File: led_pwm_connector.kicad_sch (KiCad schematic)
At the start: 7 parts, among them CN7 JST_VH_8PIN_10A_250V

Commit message: commit before updating to LiveAstra lib
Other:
- note added: "If a different signal is required here the 0Ohm + PTH will allow a post assembly fix / experimentation. Otherwise, just GND."
- note added: "Information"

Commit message: Updated library name, updated and verified all footprints
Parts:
- CN7: symbol EASYEDA2KICAD:JST_VH_8PIN_10A_250V -> LiveAstra:JST_VH_8PIN_10A_250V
- R31: symbol EASYEDA2KICAD:R_0Ohm_0805_125mW -> LiveAstra:R_0Ohm_0805_125mW
- TP55, TP56, TP57, TP58, TP59: symbol EASYEDA2KICAD:TestPoint_Thimble -> LiveAstra:TestPoint_Thimble
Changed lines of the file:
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@@
 	)
 	(symbol
-		(lib_id "EASYEDA2KICAD:JST_VH_8PIN_10A_250V")
+		(lib_id "LiveAstra:JST_VH_8PIN_10A_250V")
 		(at 182.88 96.52 0)
 		(unit 1)
@@
 	)
 	(symbol
-		(lib_id "EASYEDA2KICAD:TestPoint_Thimble")
+		(lib_id "LiveAstra:TestPoint_Thimble")
 		(at 121.92 78.74 0)
 		(unit 1)
@@
 	)
 	(symbol
-		(lib_id "EASYEDA2KICAD:+5V_IN")
+		(lib_id "LiveAstra:+5V_IN")
 		(at 172.72 76.2 0)
 		(unit 1)
@@
 	)
 	(symbol
-		(lib_id "EASYEDA2KICAD:R_0Ohm_0805_125mW")
+		(lib_id "LiveAstra:R_0Ohm_0805_125mW")
 		(at 121.92 116.84 0)
 		(unit 1)
@@
 	)
 	(symbol
-		(lib_id "EASYEDA2KICAD:TestPoint_Thimble")
+		(lib_id "LiveAstra:TestPoint_Thimble")
 		(at 86.36 78.74 0)
 		(unit 1)
@@
 	)
 	(symbol
-		(lib_id "EASYEDA2KICAD:TestPoint_Thimble")
+		(lib_id "LiveAstra:TestPoint_Thimble")
 		(at 152.4 78.74 0)
 		(unit 1)
@@
 	)
 	(symbol
-		(lib_id "EASYEDA2KICAD:TestPoint_Thimble")
+		(lib_id "LiveAstra:TestPoint_Thimble")
 		(at 55.88 78.74 0)
 		(unit 1)
@@
 	)
 	(symbol
-		(lib_id "EASYEDA2KICAD:TestPoint_Thimble")
+		(lib_id "LiveAstra:TestPoint_Thimble")
 		(at 139.7 114.3 0)
 		(unit 1)

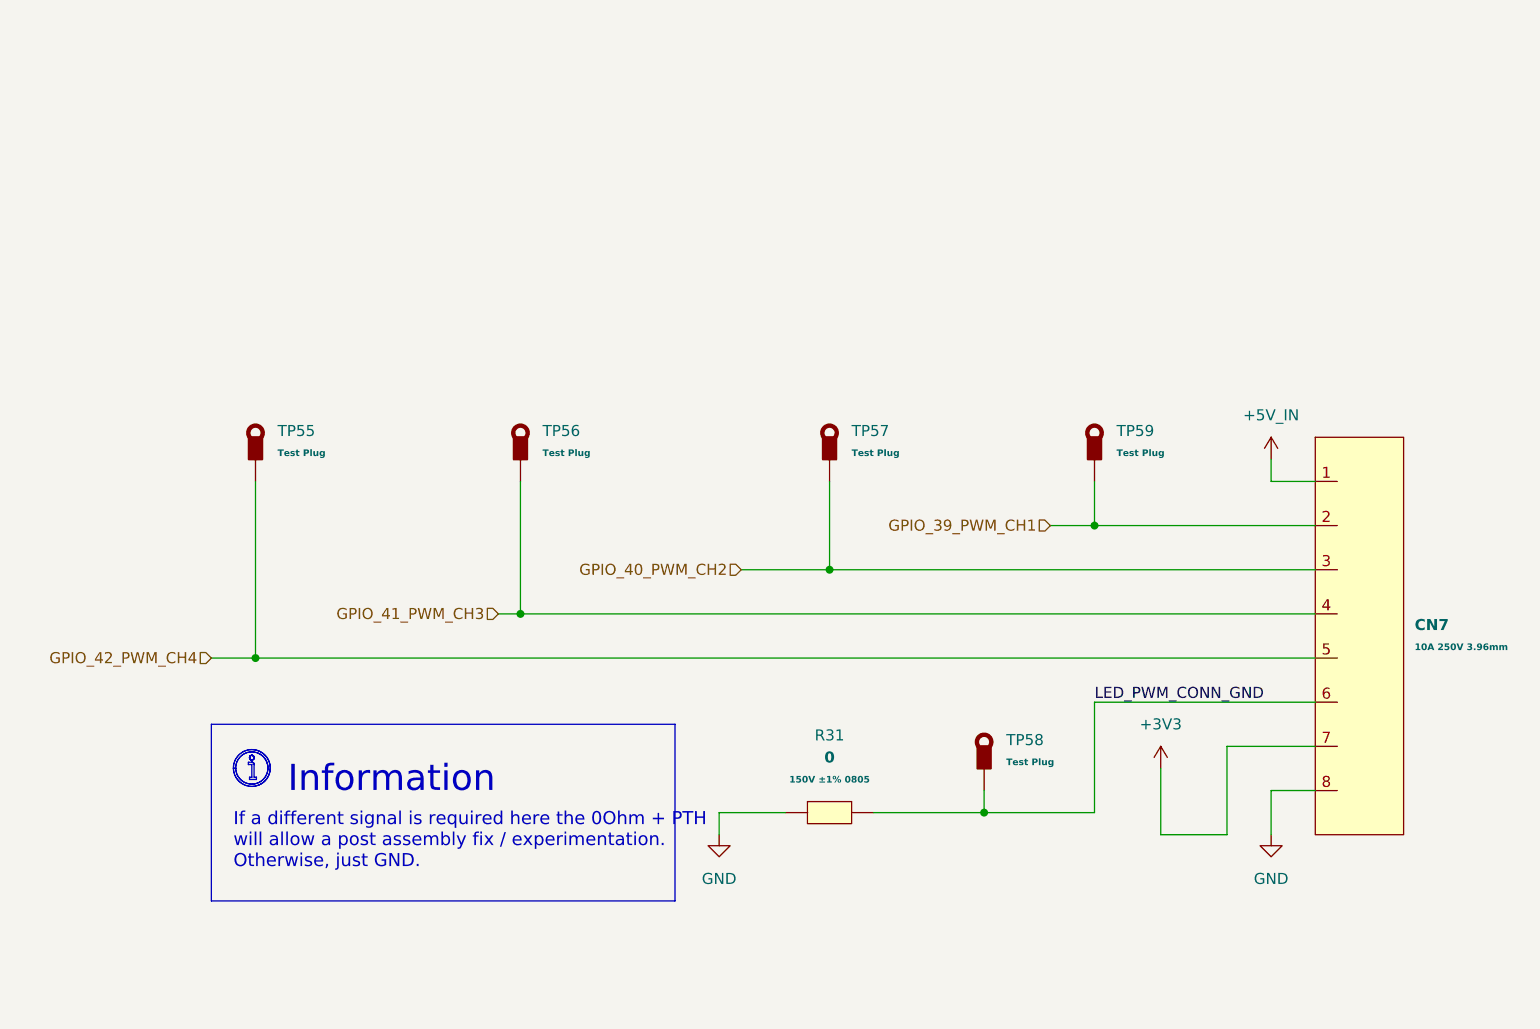
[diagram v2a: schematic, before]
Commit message: Finished layout no drc or erc errors
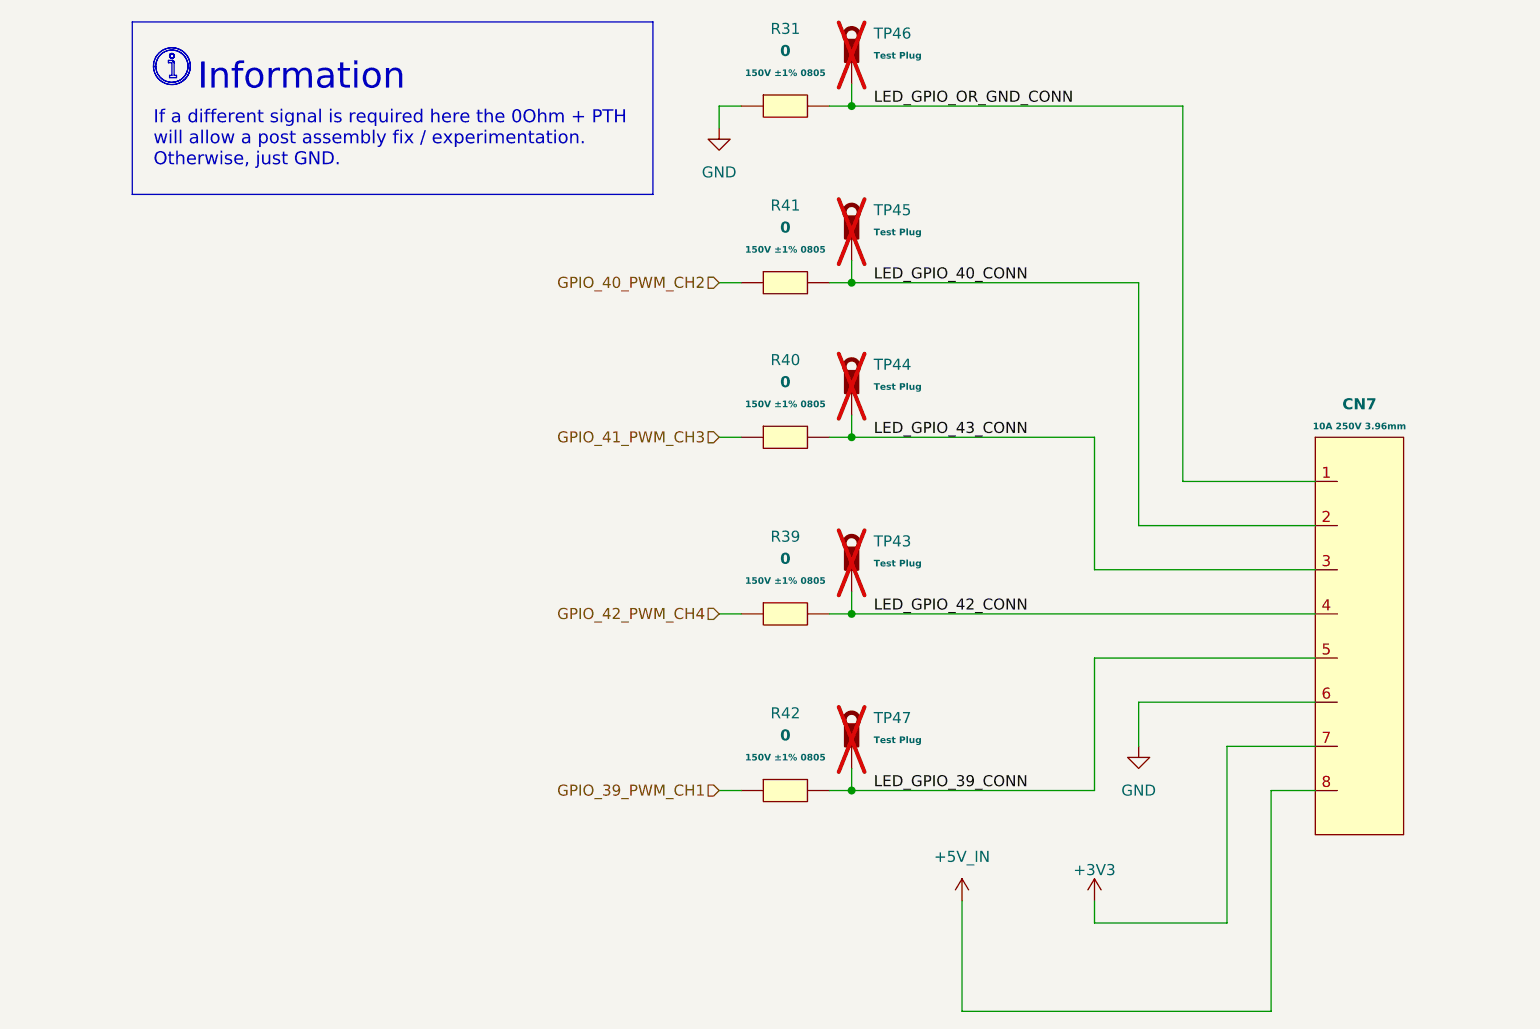
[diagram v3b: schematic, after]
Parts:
- added R39, R40, R41, R42: 0, LiveAstra:R_0805_2012Metric_Pad1.20x1.40mm_HandSolder, symbol LiveAstra:R_0Ohm_0805_125mW
- CN7: footprint Connector_JST:JST_VH_B8P-VH-B_1x08_P3.96mm_Vertical -> LiveAstra:JST_VH_B8P-VH-B_1x08_P3.96mm_Vertical
- R31: footprint Resistor_SMD:R_0805_2012Metric_Pad1.20x1.40mm_HandSolder -> LiveAstra:R_0805_2012Metric_Pad1.20x1.40mm_HandSolder
- TP43: renamed from TP55; footprint TestPoint:TestPoint_Loop_D3.50mm_Drill0.9mm_Beaded -> LiveAstra:TestPoint_Loop_D3.50mm_Drill0.9mm_Beaded; now not fitted; now left out of the parts list
- TP44: renamed from TP56; footprint TestPoint:TestPoint_Loop_D3.50mm_Drill0.9mm_Beaded -> LiveAstra:TestPoint_Loop_D3.50mm_Drill0.9mm_Beaded; now not fitted; now left out of the parts list
- TP45: renamed from TP57; footprint TestPoint:TestPoint_Loop_D3.50mm_Drill0.9mm_Beaded -> LiveAstra:TestPoint_Loop_D3.50mm_Drill0.9mm_Beaded; now not fitted; now left out of the parts list
- TP46: renamed from TP58; footprint TestPoint:TestPoint_Loop_D3.50mm_Drill0.9mm_Beaded -> LiveAstra:TestPoint_Loop_D3.50mm_Drill0.9mm_Beaded; now not fitted; now left out of the parts list
- TP47: renamed from TP59; footprint TestPoint:TestPoint_Loop_D3.50mm_Drill0.9mm_Beaded -> LiveAstra:TestPoint_Loop_D3.50mm_Drill0.9mm_Beaded; now not fitted; now left out of the parts list
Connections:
- net +5V_IN: now also CN7.8; no longer CN7.1
- net GND: now also CN7.6; no longer CN7.8
- net GPIO_39_PWM_CH1: now also R42.1; no longer CN7.2, TP47.1
- net GPIO_40_PWM_CH2: now also R41.1; no longer CN7.3, TP45.1
- net GPIO_41_PWM_CH3: now also R40.1; no longer CN7.4, TP44.1
- net GPIO_42_PWM_CH4: now also R39.1; no longer CN7.5, TP43.1
- net LED_PWM_CONN_GND renamed LED_GPIO_OR_GND_CONN
- net LED_GPIO_OR_GND_CONN: now also CN7.1; no longer CN7.6
- new net LED_GPIO_39_CONN: CN7.5, R42.2, TP47.1
- new net LED_GPIO_40_CONN: CN7.2, R41.2, TP45.1
- new net LED_GPIO_42_CONN: CN7.4, R39.2, TP43.1
- new net LED_GPIO_43_CONN: CN7.3, R40.2, TP44.1
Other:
- moved on the sheet: R31

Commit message: Ready for kibot
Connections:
- net GPIO_39_PWM_CH1 renamed PWM_CH4
- net GPIO_40_PWM_CH2 renamed PWM_CH1
- net GPIO_41_PWM_CH3 renamed PWM_CH2
- net GPIO_42_PWM_CH4 renamed PWM_CH3
- net LED_GPIO_39_CONN renamed PWM_CH4_CONN
- net LED_GPIO_40_CONN renamed PWM_CH1_CONN
- net LED_GPIO_42_CONN renamed PWM_CH3_CONN
- net LED_GPIO_43_CONN renamed PWM_CH2_CONN
- net LED_GPIO_OR_GND_CONN renamed LED_EXTRA_PIN
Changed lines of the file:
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@@
 		)
 	)
-	(label "LED_GPIO_39_CONN"
+	(label "PWM_CH4_CONN"
 		(at 127 114.3 0)
 		(fields_autoplaced yes)
@@
 		)
 	)
-	(label "LED_GPIO_40_CONN"
+	(label "PWM_CH1_CONN"
 		(at 127 55.88 0)
 		(fields_autoplaced yes)
@@
 		)
 	)
-	(label "LED_GPIO_OR_GND_CONN"
+	(label "LED_EXTRA_PIN"
 		(at 127 35.56 0)
 		(fields_autoplaced yes)
@@
 		)
 	)
-	(label "LED_GPIO_42_CONN"
+	(label "PWM_CH3_CONN"
 		(at 127 93.98 0)
 		(fields_autoplaced yes)
@@
 		)
 	)
-	(label "LED_GPIO_43_CONN"
+	(label "PWM_CH2_CONN"
 		(at 127 73.66 0)
 		(fields_autoplaced yes)
@@
 		)
 	)
-	(hierarchical_label "GPIO_41_PWM_CH3"
+	(hierarchical_label "PWM_CH3"
+		(shape input)
+		(at 109.22 93.98 180)
+		(fields_autoplaced yes)
+		(effects
+			(font
+				(size 1.27 1.27)
+			)
+			(justify right)
+		)
+	)
+	(hierarchical_label "PWM_CH2"
 		(shape input)
 		(at 109.22 73.66 180)
@@
 		)
 	)
-	(hierarchical_label "GPIO_42_PWM_CH4"
+	(hierarchical_label "PWM_CH4"
 		(shape input)
-		(at 109.22 93.98 180)
+		(at 109.22 114.3 180)
 		(fields_autoplaced yes)
 		(effects
@@
 		)
 	)
-	(hierarchical_label "GPIO_40_PWM_CH2"
+	(hierarchical_label "PWM_CH1"
 		(shape input)
 		(at 109.22 55.88 180)
 		(fields_autoplaced yes)
 		(effects
-			(font
-				(size 1.27 1.27)
-			)
-			(justify right)
-		)
-	)
-	(hierarchical_label "GPIO_39_PWM_CH1"
-		(shape input)
-		(at 109.22 114.3 180)
-		(fields_autoplaced yes)
-		(effects

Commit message: Work on kibot
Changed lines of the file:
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@@
-		)
-	)
-	(polyline
-		(pts
-			(xy 46.2731 30.3055) (xy 46.2861 30.3065) (xy 46.299 30.3081) (xy 46.3118 30.3103) (xy 46.3245 30.3132)
-			(xy 46.3369 30.3166) (xy 46.3492 30.3207) (xy 46.3612 30.3253) (xy 46.373 30.3306) (xy 46.3846 30.3364)
-			(xy 46.3958 30.3427) (xy 46.4068 30.3497) (xy 46.4174 30.3571) (xy 46.4276 30.3651) (xy 46.4375 30.3737)
-			(xy 46.4471 30.3827) (xy 46.4561 30.3922) (xy 46.4646 30.4021) (xy 46.4726 30.4124) (xy 46.4801 30.423)
-			(xy 46.487 30.4339) (xy 46.4934 30.4452) (xy 46.4992 30.4567) (xy 46.5044 30.4685) (xy 46.5091 30.4806)
-			(xy 46.5131 30.4928) (xy 46.5166 30.5053) (xy 46.5194 30.5179) (xy 46.5217 30.5307) (xy 46.5233 30.5436)
-			(xy 46.5242 30.5567) (xy 46.5245 30.5698) (xy 46.5245 32.025) (xy 46.7891 32.025) (xy 46.7891 32.2896)
-			(xy 45.9954 32.2896) (xy 45.9954 32.025) (xy 46.26 32.025) (xy 46.26 30.5698) (xy 45.8631 30.5698)
-			(xy 45.8631 30.3052) (xy 46.26 30.3052) (xy 46.2731 30.3055)
-		)
-		(stroke
-			(width -0.0001)
-			(type solid)
-		)
-		(fill
-			(type color)
-			(color 34 187 51 1)
-		)
-	)
-	(polyline
-		(pts
-			(xy 46.2736 29.5118) (xy 46.287 29.5128) (xy 46.3003 29.5145) (xy 46.3133 29.5168) (xy 46.3261 29.5198)
-			(xy 46.3386 29.5234) (xy 46.3509 29.5275) (xy 46.363 29.5323) (xy 46.3747 29.5375) (xy 46.3861 29.5434)
-			(xy 46.3972 29.5498) (xy 46.4079 29.5566) (xy 46.4183 29.564) (xy 46.4283 29.5719) (xy 46.4379 29.5802)
-			(xy 46.4471 29.589) (xy 46.4558 29.5981) (xy 46.4641 29.6077) (xy 46.472 29.6177) (xy 46.4794 29.6281)
-			(xy 46.4862 29.6388) (xy 46.4926 29.6499) (xy 46.4985 29.6613) (xy 46.5038 29.6731) (xy 46.5085 29.6851)
-			(xy 46.5127 29.6974) (xy 46.5162 29.7099) (xy 46.5192 29.7227) (xy 46.5215 29.7357) (xy 46.5232 29.749)
-			(xy 46.5242 29.7624) (xy 46.5245 29.776) (xy 46.5242 29.7897) (xy 46.5232 29.8031) (xy 46.5215 29.8163)
-			(xy 46.5192 29.8294) (xy 46.5162 29.8422) (xy 46.5127 29.8547) (xy 46.5085 29.867) (xy 46.5038 29.879)
-			(xy 46.4985 29.8907) (xy 46.4926 29.9022) (xy 46.4862 29.9132) (xy 46.4794 29.924) (xy 46.472 29.9343)
-			(xy 46.4641 29.9443) (xy 46.4558 29.9539) (xy 46.4471 29.9631) (xy 46.4379 29.9719) (xy 46.4283 29.9802)
-			(xy 46.4183 29.9881) (xy 46.4079 29.9954) (xy 46.3972 30.0023) (xy 46.3861 30.0087) (xy 46.3747 30.0145)
-			(xy 46.363 30.0198) (xy 46.3509 30.0246) (xy 46.3386 30.0287) (xy 46.3261 30.0323) (xy 46.3133 30.0352)
-			(xy 46.3003 30.0376) (xy 46.287 30.0393) (xy 46.2736 30.0403) (xy 46.26 30.0406) (xy 46.2464 30.0403)
-			(xy 46.2329 30.0393) (xy 46.2197 30.0376) (xy 46.2066 30.0352) (xy 46.1938 30.0323) (xy 46.1813 30.0287)
-			(xy 46.169 30.0246) (xy 46.157 30.0198) (xy 46.1453 30.0145) (xy 46.1339 30.0087) (xy 46.1228 30.0023)
-			(xy 46.112 29.9954) (xy 46.1017 29.9881) (xy 46.0917 29.9802) (xy 46.0821 29.9719) (xy 46.0729 29.9631)
-			(xy 46.0641 29.9539) (xy 46.0558 29.9443) (xy 46.0479 29.9343) (xy 46.0406 29.924) (xy 46.0337 29.9132)
-			(xy 46.0273 29.9022) (xy 46.0215 29.8907) (xy 46.0162 29.879) (xy 46.0114 29.867) (xy 46.0073 29.8547)
-			(xy 46.0037 29.8422) (xy 46.0008 29.8294) (xy 45.9984 29.8163) (xy 45.9967 29.8031) (xy 45.9957 29.7897)
-			(xy 45.9954 29.776) (xy 45.9957 29.7624) (xy 45.9967 29.749) (xy 45.9984 29.7357) (xy 46.0008 29.7227)
-			(xy 46.0037 29.7099) (xy 46.0073 29.6974) (xy 46.0114 29.6851) (xy 46.0162 29.6731) (xy 46.0215 29.6613)
-			(xy 46.0273 29.6499) (xy 46.0337 29.6388) (xy 46.0406 29.6281) (xy 46.0479 29.6177) (xy 46.0558 29.6077)
-			(xy 46.0641 29.5981) (xy 46.0729 29.589) (xy 46.0821 29.5802) (xy 46.0917 29.5719) (xy 46.1017 29.564)
-			(xy 46.112 29.5566) (xy 46.1228 29.5498) (xy 46.1339 29.5434) (xy 46.1453 29.5375) (xy 46.157 29.5323)
-			(xy 46.169 29.5275) (xy 46.1813 29.5234) (xy 46.1938 29.5198) (xy 46.2066 29.5168) (xy 46.2197 29.5145)
-			(xy 46.2329 29.5128) (xy 46.2464 29.5118) (xy 46.26 29.5115) (xy 46.2736 29.5118)
-		)
-		(stroke
-			(width -0.0001)
-			(type solid)
-		)
-		(fill
-			(type color)
-			(color 34 187 51 1)
-		)
-	)
-	(polyline
-		(pts
-			(xy 46.3649 28.8526) (xy 46.4692 28.8604) (xy 46.5725 28.8732) (xy 46.6748 28.891) (xy 46.7759 28.9138)
-			(xy 46.8756 28.9415) (xy 46.9737 28.9739) (xy 47.07 29.0111) (xy 47.1644 29.0529) (xy 47.2567 29.0994)
-			(xy 47.3467 29.1503) (xy 47.4343 29.2056) (xy 47.5193 29.2653) (xy 47.6014 29.3293) (xy 47.6806 29.3976)
-			(xy 47.7567 29.47) (xy 47.8291 29.546) (xy 47.8973 29.6252) (xy 47.9613 29.7074) (xy 48.021 29.7923)
-			(xy 48.0764 29.8799) (xy 48.1273 29.9699) (xy 48.1737 30.0623) (xy 48.2155 30.1567) (xy 48.2527 30.253)
-			(xy 48.2851 30.3511) (xy 48.3128 30.4507) (xy 48.3356 30.5518) (xy 48.3534 30.6541) (xy 48.3663 30.7575)
-			(xy 48.374 30.8617) (xy 48.3766 30.9667) (xy 48.3751 31.0467) (xy 48.3706 31.1261) (xy 48.3632 31.2049)
-			(xy 48.3529 31.2831) (xy 48.3398 31.3604) (xy 48.3238 31.437) (xy 48.3051 31.5126) (xy 48.2837 31.5873)
-			(xy 48.2596 31.661) (xy 48.2329 31.7336) (xy 48.2036 31.805) (xy 48.1717 31.8752) (xy 48.1374 31.9442)
-			(xy 48.1006 32.0118) (xy 48.0615 32.0779) (xy 48.0199 32.1426) (xy 47.976 32.2058) (xy 47.9299 32.2673)
-			(xy 47.8815 32.3271) (xy 47.831 32.3852) (xy 47.7783 32.4415) (xy 47.7235 32.4959) (xy 47.6667 32.5484)
-			(xy 47.6078 32.5988) (xy 47.547 32.6472) (xy 47.4843 32.6934) (xy 47.4197 32.7375) (xy 47.3532 32.7792)
-			(xy 47.285 32.8187) (xy 47.215 32.8557) (xy 47.1433 32.8902) (xy 47.07 32.9222) (xy 46.9204 32.9777)
-			(xy 46.7686 33.0214) (xy 46.6153 33.0534) (xy 46.461 33.0739) (xy 46.3064 33.0829) (xy 46.1522 33.0806)
-			(xy 45.9988 33.0672) (xy 45.847 33.0427) (xy 45.6974 33.0072) (xy 45.5506 32.961) (xy 45.4072 32.904)
-			(xy 45.2678 32.8365) (xy 45.1331 32.7586) (xy 45.0037 32.6703) (xy 44.8802 32.5719) (xy 44.7633 32.4634)
-			(xy 44.6547 32.3464) (xy 44.5563 32.2229) (xy 44.468 32.0935) (xy 44.3901 31.9588) (xy 44.3226 31.8194)
-			(xy 44.2657 31.676) (xy 44.2194 31.5292) (xy 44.184 31.3796) (xy 44.1595 31.2278) (xy 44.146 31.0745)
-			(xy 44.145 31.0073) (xy 44.4083 31.0073) (xy 44.4162 31.1426) (xy 44.4341 31.2776) (xy 44.4621 31.4117)
-			(xy 44.5003 31.5445) (xy 44.5489 31.6754) (xy 44.6071 31.8023) (xy 44.674 31.9233) (xy 44.749 32.0379)
-			(xy 44.8318 32.146) (xy 44.9219 32.2473) (xy 45.0187 32.3413) (xy 45.1219 32.4279) (xy 45.231 32.5066)
-			(xy 45.3455 32.5773) (xy 45.465 32.6395) (xy 45.5889 32.693) (xy 45.7169 32.7374) (xy 45.8485 32.7725)
-			(xy 45.9831 32.798) (xy 46.1205 32.8135) (xy 46.26 32.8187) (xy 46.3518 32.8165) (xy 46.443 32.8097)
-			(xy 46.5335 32.7985) (xy 46.623 32.7828) (xy 46.7114 32.7629) (xy 46.7986 32.7387) (xy 46.8844 32.7103)
-			(xy 46.9687 32.6778) (xy 47.0513 32.6412) (xy 47.1321 32.6006) (xy 47.2109 32.556) (xy 47.2875 32.5076)
-			(xy 47.3618 32.4553) (xy 47.4337 32.3993) (xy 47.503 32.3396) (xy 47.5696 32.2763) (xy 47.6329 32.2097)
-			(xy 47.6926 32.1404) (xy 47.7486 32.0685) (xy 47.8009 31.9942) (xy 47.8493 31.9176) (xy 47.8939 31.8388)
-			(xy 47.9345 31.758) (xy 47.9711 31.6754) (xy 48.0036 31.5911) (xy 48.032 31.5053) (xy 48.0562 31.4181)
-			(xy 48.0761 31.3297) (xy 48.0918 31.2402) (xy 48.103 31.1497) (xy 48.1098 31.0585) (xy 48.112 30.9667)
-			(xy 48.1107 30.8967) (xy 48.1068 30.8272) (xy 48.1003 30.7582) (xy 48.0913 30.6898) (xy 48.0798 30.6221)
-			(xy 48.0658 30.5552) (xy 48.0495 30.489) (xy 48.0307 30.4236) (xy 48.0096 30.3591) (xy 47.9863 30.2956)
-			(xy 47.9606 30.2331) (xy 47.9328 30.1717) (xy 47.9027 30.1113) (xy 47.8706 30.0522) (xy 47.8363 29.9943)
-			(xy 47.7999 29.9377) (xy 47.7615 29.8825) (xy 47.7212 29.8286) (xy 47.6788 29.7763) (xy 47.6346 29.7254)
-			(xy 47.5885 29.6762) (xy 47.5406 29.6286) (xy 47.4908 29.5827) (xy 47.4393 29.5385) (xy 47.3861 29.4962)
-			(xy 47.3312 29.4557) (xy 47.2747 29.4172) (xy 47.2166 29.3807) (xy 47.1569 29.3462) (xy 47.0956 29.3138)
-			(xy 47.0329 29.2836) (xy 46.9687 29.2556) (xy 46.8378 29.207) (xy 46.705 29.1688) (xy 46.5709 29.1408)
-			(xy 46.4359 29.1229) (xy 46.3006 29.115) (xy 46.1656 29.117) (xy 46.0315 29.1287) (xy 45.8986 29.1502)
-			(xy 45.7677 29.1812) (xy 45.6393 29.2217) (xy 45.5138 29.2715) (xy 45.3919 29.3305) (xy 45.274 29.3987)
-			(xy 45.1608 29.476) (xy 45.0527 29.5621) (xy 44.9503 29.657) (xy 44.8554 29.7594) (xy 44.7693 29.8675)
-			(xy 44.692 29.9807) (xy 44.6238 30.0986) (xy 44.5648 30.2205) (xy 44.515 30.346) (xy 44.4745 30.4744)
-			(xy 44.4435 30.6053) (xy 44.422 30.7382) (xy 44.4103 30.8723) (xy 44.4083 31.0073) (xy 44.145 31.0073)
-			(xy 44.1437 30.9202) (xy 44.1528 30.7656) (xy 44.1732 30.6114) (xy 44.2052 30.458) (xy 44.2489 30.3063)
-			(xy 44.3044 30.1567) (xy 44.371 30.0116) (xy 44.4474 29.8734) (xy 44.5332 29.7424) (xy 44.6278 29.6188)
-			(xy 44.7307 29.5031) (xy 44.8414 29.3956) (xy 44.9593 29.2967) (xy 45.084 29.2067) (xy 45.2149 29.126)
-			(xy 45.3514 29.0549) (xy 45.493 28.9937) (xy 45.6393 28.9429) (xy 45.7897 28.9028) (xy 45.9436 28.8737)
-			(xy 46.1005 28.856) (xy 46.26 28.85) (xy 46.3649 28.8526)
-		)
-		(stroke
-			(width -0.0001)
-			(type solid)
-		)
-		(fill
-			(type color)
-			(color 34 187 51 1)
 		)
 	)
